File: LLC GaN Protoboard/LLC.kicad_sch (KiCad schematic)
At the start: 45 parts, among them IC1 FAN73912AMX, IC2 BZX84-C5V6,215, IC3 BZX84-C5V6,215, IC4 GAN7R0-150LBE, IC5 GAN7R0-150LBE, IC6 BZX84-C5V6,215, U1 PLMR54410DBVR

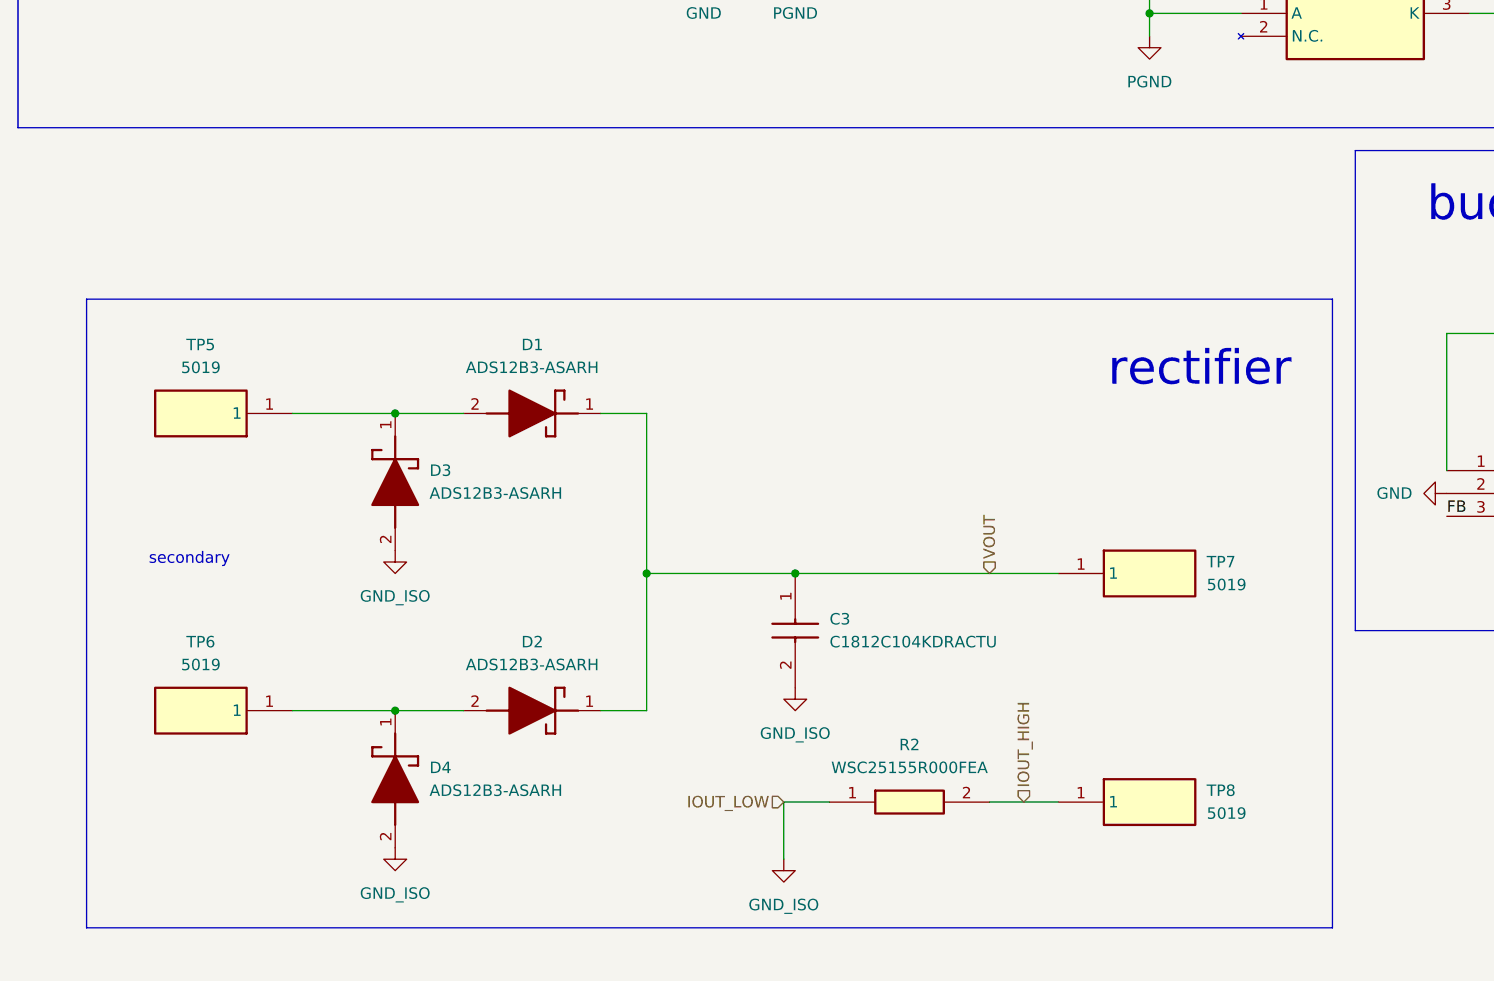
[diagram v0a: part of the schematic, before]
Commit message: Added secondary clamp and swapped components
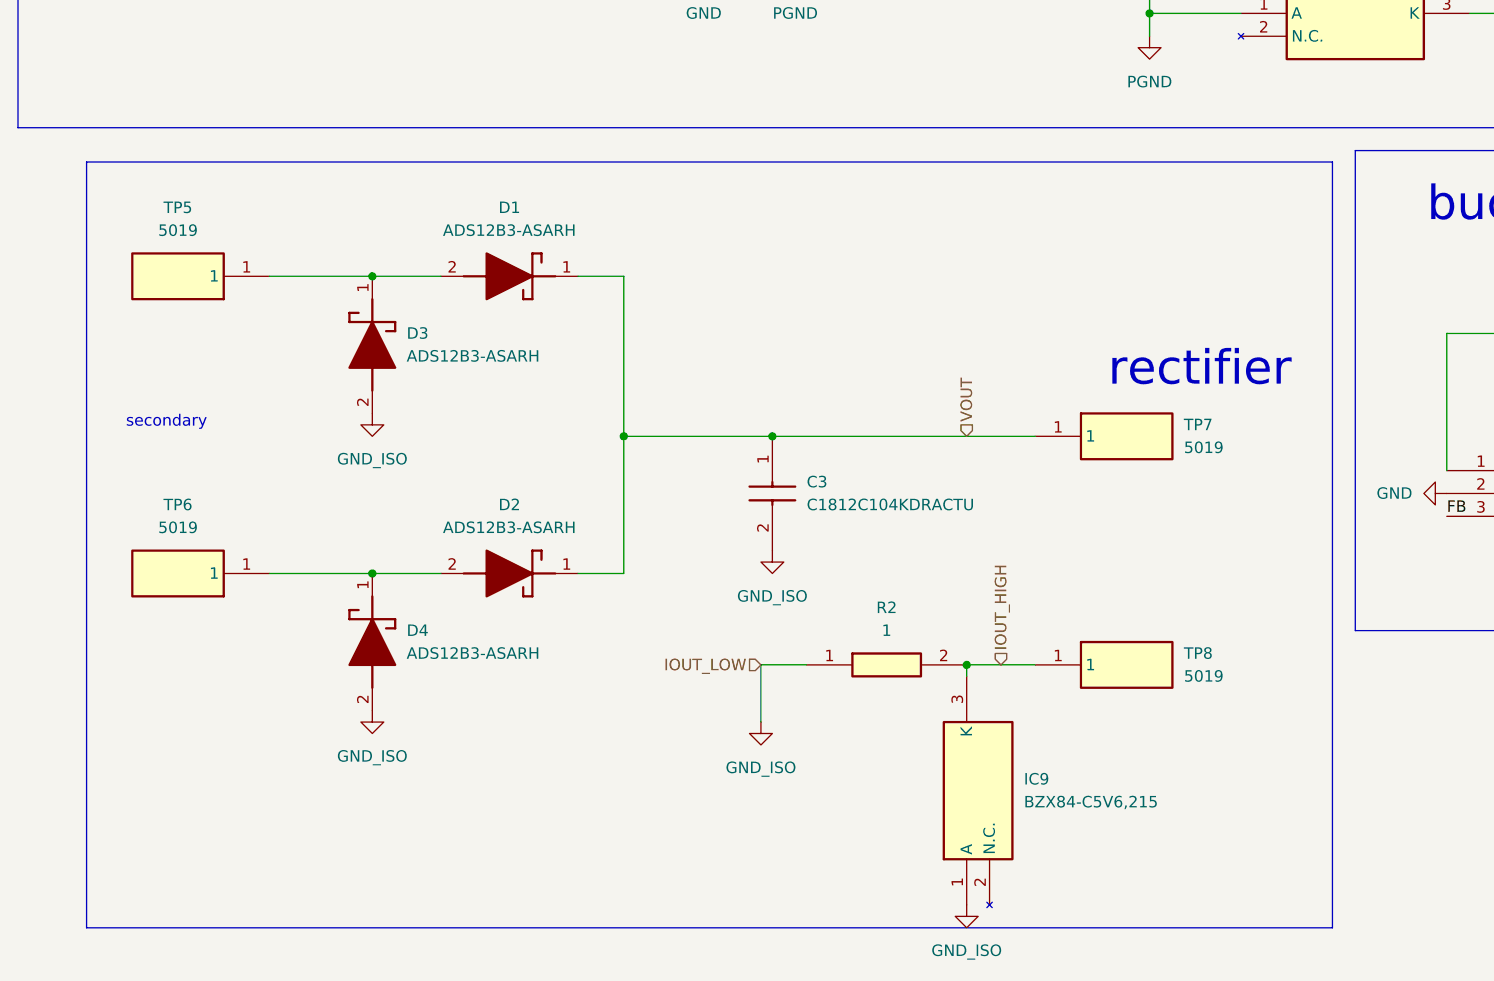
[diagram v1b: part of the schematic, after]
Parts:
- added IC9: BZX84-C5V6,215, BZX84-C5V6,215:SOT95P230X110-3N, symbol BZX84-C5V6_215:BZX84-C5V6,215
- R2: value WSC25155R000FEA -> 1
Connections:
- net GND_ISO: now also IC9.1 (A)
- net IOUT_HIGH: now also IC9.3 (K)
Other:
- moved on the sheet: C3, D1, D2, D3, D4, R2, TP5, TP6, TP7, TP8
